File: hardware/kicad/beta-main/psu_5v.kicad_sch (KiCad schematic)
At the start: 0 parts

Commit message: tweaks and added servo controller
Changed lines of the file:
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@@
+		)
+	)
+	(hierarchical_label "VIN"
+		(shape input)
+		(at 49.53 45.72 0)
+		(effects
+			(font
+				(size 1.27 1.27)
+			)
+			(justify left)
 		)
 	)

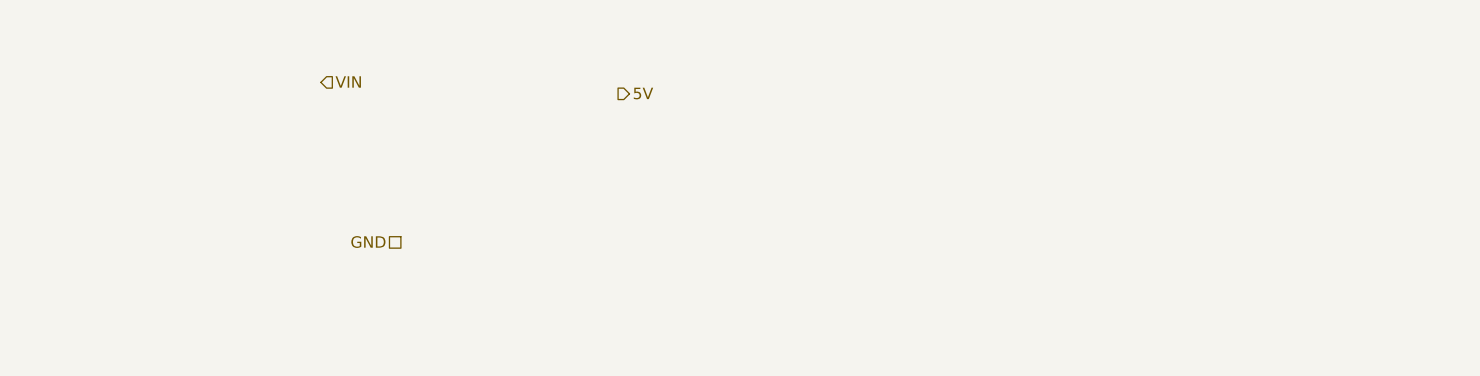
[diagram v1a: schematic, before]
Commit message: add 5v power supply
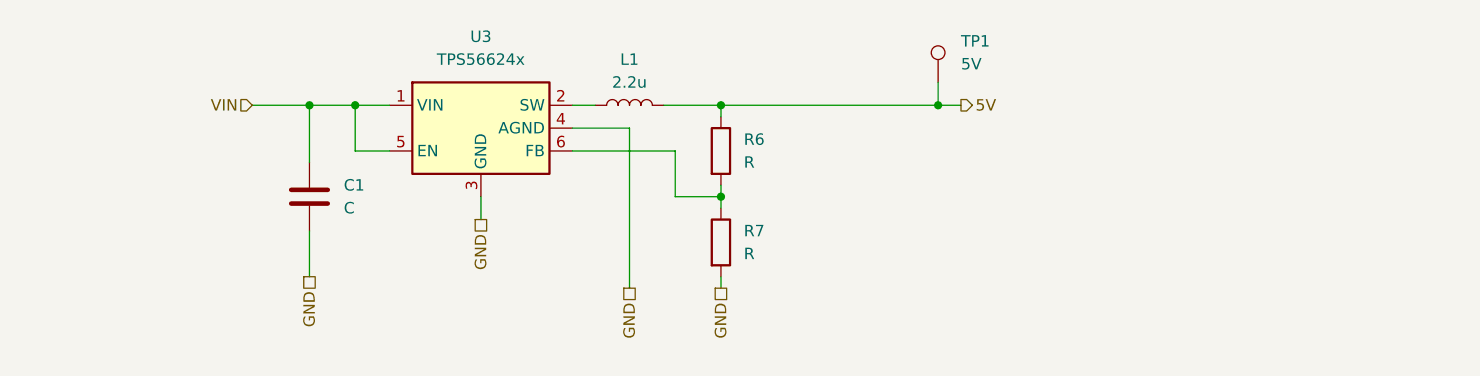
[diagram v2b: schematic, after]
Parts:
- added C1: C, symbol Device:C
- added L1: 2.2u, symbol Device:L
- added R6, R7: R, symbol Device:R
- added TP1: 5V, symbol Connector:TestPoint
- added U3: TPS56624x, Package_TO_SOT_SMD:SOT-563, symbol Beta:TPS56624x
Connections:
- net 5V: now also L1.2, R6.1, TP1.1
- net GND: now also C1.2, R7.2, U3.3 (GND), U3.4 (AGND)
- net VIN: now also C1.1, U3.1 (VIN), U3.5 (EN)
- new net: R6.2, R7.1, U3.6 (FB)
- new net: L1.1, U3.2 (SW)

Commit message: 5V and amplifier corrections
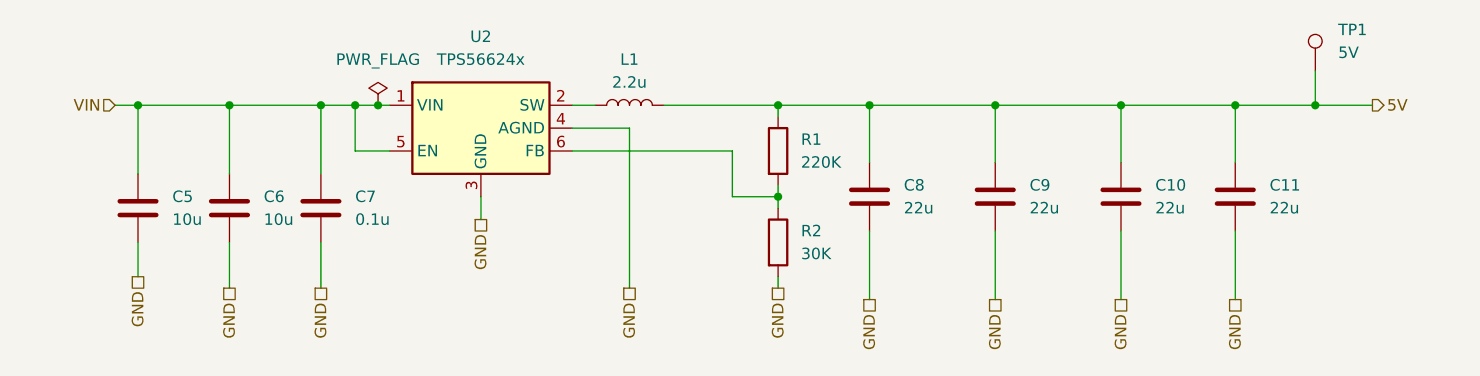
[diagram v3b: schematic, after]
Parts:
- added C10, C11, C8, C9: 22u, symbol Device:C
- added C6: 10u, symbol Device:C
- added C7: 0.1u, symbol Device:C
- C5: renamed from C1; value C -> 10u
- R1: renamed from R6; value R -> 220K
- R2: renamed from R7; value R -> 30K
- renumbered U3 to U2
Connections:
- net 5V: now also C10.1, C11.1, C8.1, C9.1
- net GND: now also C10.2, C11.2, C6.2, C7.2, C8.2, C9.2
- net VIN: now also C6.1, C7.1
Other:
- moved on the sheet: C5, R1, R2, TP1

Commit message: Setup for PCB layout
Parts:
- C10, C11, C5, C6, C8, C9: footprint (none) -> Capacitor_SMD:C_0805_2012Metric
- C7: footprint (none) -> Capacitor_SMD:C_0402_1005Metric
- L1: footprint (none) -> CM5IO:L_Bourns_SRP5030CC
- R1, R2: footprint (none) -> Resistor_SMD:R_0402_1005Metric
- TP1: footprint (none) -> TestPoint:TestPoint_Pad_D1.0mm
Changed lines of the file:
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@@
 			)
 		)
-		(property "Footprint" ""
+		(property "Footprint" "Resistor_SMD:R_0402_1005Metric"
 			(at 98.552 63.5 90)
 			(effects
@@
 			)
 		)
-		(property "Footprint" ""
+		(property "Footprint" "CM5IO:L_Bourns_SRP5030CC"
 			(at 83.82 48.26 0)
 			(effects
@@
 			)
 		)
-		(property "Footprint" ""
+		(property "Footprint" "TestPoint:TestPoint_Pad_D1.0mm"
 			(at 165.1 44.45 0)
 			(effects
@@
 			)
 		)
-		(property "Footprint" ""
+		(property "Footprint" "Capacitor_SMD:C_0805_2012Metric"
 			(at 111.4552 62.23 0)
 			(effects
@@
 			)
 		)
-		(property "Footprint" ""
+		(property "Footprint" "Capacitor_SMD:C_0805_2012Metric"
 			(at 125.4252 62.23 0)
 			(effects
@@
 			)
 		)
-		(property "Footprint" ""
+		(property "Footprint" "Capacitor_SMD:C_0402_1005Metric"
 			(at 50.4952 63.5 0)
 			(effects
@@
 			)
 		)
-		(property "Footprint" ""
+		(property "Footprint" "Capacitor_SMD:C_0805_2012Metric"
 			(at 139.3952 62.23 0)
 			(effects
@@
 			)
 		)
-		(property "Footprint" ""
+		(property "Footprint" "Capacitor_SMD:C_0805_2012Metric"
 			(at 40.3352 63.5 0)
 			(effects
@@
 			)
 		)
-		(property "Footprint" ""
+		(property "Footprint" "Resistor_SMD:R_0402_1005Metric"
 			(at 98.552 53.34 90)
 			(effects
@@
 			)
 		)
-		(property "Footprint" ""
+		(property "Footprint" "Capacitor_SMD:C_0805_2012Metric"
 			(at 30.1752 63.5 0)
 			(effects
@@
 			)
 		)
-		(property "Footprint" ""
+		(property "Footprint" "Capacitor_SMD:C_0805_2012Metric"
 			(at 152.0952 62.23 0)
 			(effects

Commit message: remove power symbols from hierarchy and move different subsystems  around
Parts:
- L1: footprint CM5IO:L_Bourns_SRP5030CC -> Inductor_SMD:L_Bourns_SRP5030T
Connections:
- net 5V renamed +5V
- net VIN renamed +BATT
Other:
- moved on the sheet: TP1

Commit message: Footprints changed to 603
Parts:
- C10, C11, C5, C6, C8, C9: footprint Capacitor_SMD:C_0805_2012Metric -> Capacitor_SMD:C_0603_1608Metric_Pad1.08x0.95mm_HandSolder
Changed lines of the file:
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@@
 			)
 		)
-		(property "Footprint" "Capacitor_SMD:C_0805_2012Metric"
+		(property "Footprint" "Capacitor_SMD:C_0603_1608Metric_Pad1.08x0.95mm_HandSolder"
 			(at 111.4552 62.23 0)
 			(effects
@@
 			)
 		)
-		(property "Footprint" "Capacitor_SMD:C_0805_2012Metric"
+		(property "Footprint" "Capacitor_SMD:C_0603_1608Metric_Pad1.08x0.95mm_HandSolder"
 			(at 125.4252 62.23 0)
 			(effects
@@
 			)
 		)
-		(property "Footprint" "Capacitor_SMD:C_0805_2012Metric"
+		(property "Footprint" "Capacitor_SMD:C_0603_1608Metric_Pad1.08x0.95mm_HandSolder"
 			(at 139.3952 62.23 0)
 			(effects
@@
 			)
 		)
-		(property "Footprint" "Capacitor_SMD:C_0805_2012Metric"
+		(property "Footprint" "Capacitor_SMD:C_0603_1608Metric_Pad1.08x0.95mm_HandSolder"
 			(at 40.3352 63.5 0)
 			(effects
@@
 			)
 		)
-		(property "Footprint" "Capacitor_SMD:C_0805_2012Metric"
+		(property "Footprint" "Capacitor_SMD:C_0603_1608Metric_Pad1.08x0.95mm_HandSolder"
 			(at 30.1752 63.5 0)
 			(effects
@@
 			)
 		)
-		(property "Footprint" "Capacitor_SMD:C_0805_2012Metric"
+		(property "Footprint" "Capacitor_SMD:C_0603_1608Metric_Pad1.08x0.95mm_HandSolder"
 			(at 152.0952 62.23 0)
 			(effects

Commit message: Footprints fixed, fuse removed
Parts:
- L1: footprint Inductor_SMD:L_Bourns_SRP5030T -> CM5IO:L_Bourns_SRP5030CC
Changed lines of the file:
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@@
 			)
 		)
-		(property "Footprint" "Inductor_SMD:L_Bourns_SRP5030T"
+		(property "Footprint" "CM5IO:L_Bourns_SRP5030CC"
 			(at 83.82 48.26 0)
 			(effects
